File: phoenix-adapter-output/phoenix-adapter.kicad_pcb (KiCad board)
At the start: 2 copper layers, 16.2 x 20 mm, 2 parts, among them CON101 JST-XH

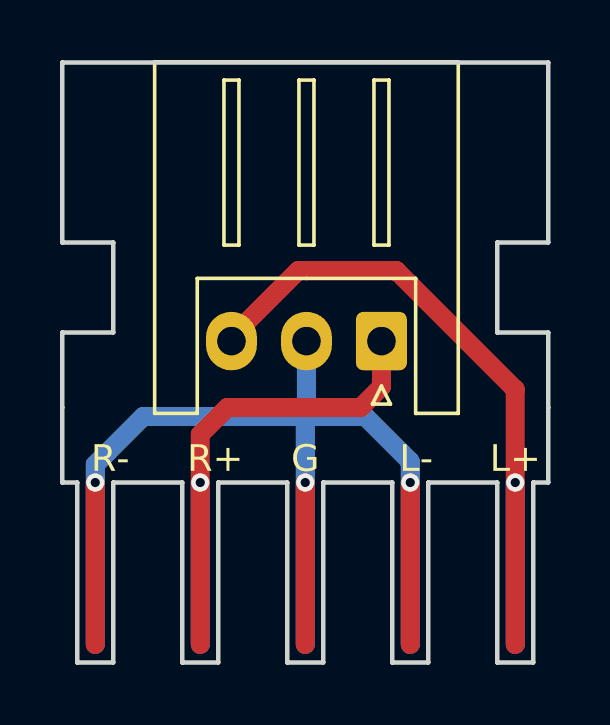
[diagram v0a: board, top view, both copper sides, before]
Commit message: added panel
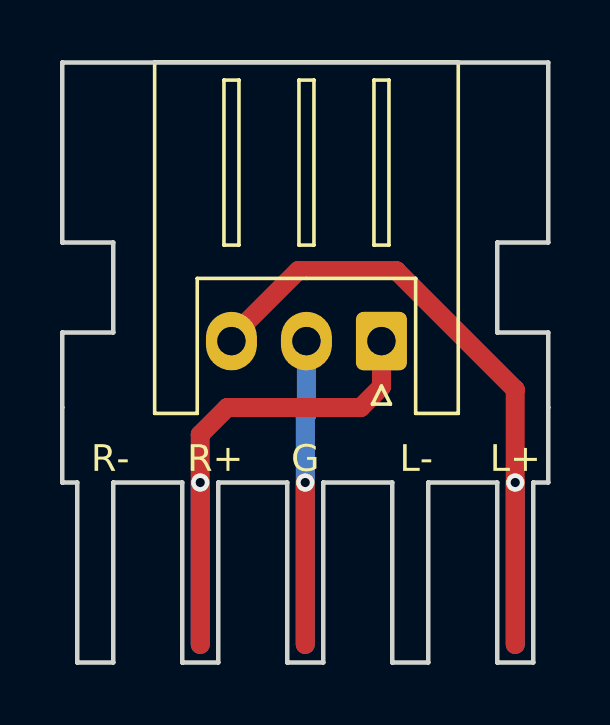
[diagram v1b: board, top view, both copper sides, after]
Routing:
- net GND: track 50.2 -> 15.5 mm, vias 3 -> 1
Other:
- board text added: "Output"
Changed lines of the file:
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@@
   (general
     (thickness 1.6)
-    (drawings 40)
-    (tracks 37)
+    (drawings 41)
+    (tracks 23)
     (zones 0)
     (modules 2)
@@
     )
   )
+  (gr_text Output (at 136.652 109.474) (layer B.SilkS)
+    (effects (font (size 1 1) (thickness 0.25)) (justify mirror))
+  )
   (gr_text db-electronics.ca (at 141.4 111.9) (layer B.SilkS)
     (effects (font (size 0.889 0.889) (thickness 0.2032)) (justify mirror))
@@
   (gr_line (start 131.6 113.3) (end 133.3 113.3) (layer Edge.Cuts) (width 0.15))
   (gr_line (start 131.6 107.3) (end 131.6 113.3) (layer Edge.Cuts) (width 0.15))
-  (segment (start 143.2 121.3) (end 143.2 126.7) (width 0.635) (layer F.Cu) (net 1))
-  (segment (start 143.2 121.3) (end 143.2 126.7) (width 0.635) (layer B.Cu) (net 1))
-  (segment (start 143.2 120.6) (end 143.2 121.3) (width 0.635) (layer B.Cu) (net 1))
-  (via (at 143.2 121.3) (size 0.6096) (drill 0.3048) (layers F.Cu B.Cu) (net 1))
   (segment (start 139.7 121.3) (end 139.7 126.7) (width 0.635) (layer F.Cu) (net 1))
   (segment (start 139.7 121.3) (end 139.7 126.7) (width 0.635) (layer B.Cu) (net 1))
   (segment (start 139.7 120.3) (end 139.7 121.3) (width 0.635) (layer B.Cu) (net 1))
   (via (at 139.7 121.3) (size 0.6096) (drill 0.3048) (layers F.Cu B.Cu) (net 1))
-  (segment (start 132.7 121.3) (end 132.7 126.7) (width 0.635) (layer F.Cu) (net 1))
-  (segment (start 132.7 121.3) (end 132.7 126.7) (width 0.635) (layer B.Cu) (net 1))
-  (segment (start 132.7 120.7) (end 132.7 121.3) (width 0.635) (layer B.Cu) (net 1))
-  (via (at 132.7 121.3) (size 0.6096) (drill 0.3048) (layers F.Cu B.Cu) (net 1))
-  (segment (start 142.9 120.3) (end 141.7 119.1) (width 0.635) (layer B.Cu) (net 1))
-  (segment (start 141.7 119.1) (end 139.7 119.1) (width 0.635) (layer B.Cu) (net 1))
   (segment (start 139.7 119.1) (end 139.7 120.3) (width 0.635) (layer B.Cu) (net 1))
-  (segment (start 133.1 120.3) (end 134.3 119.1) (width 0.635) (layer B.Cu) (net 1))
-  (segment (start 134.3 119.1) (end 139.7 119.1) (width 0.635) (layer B.Cu) (net 1))
-  (segment (start 133.1 120.3) (end 132.7 120.7) (width 0.635) (layer B.Cu) (net 1))
-  (segment (start 142.9 120.3) (end 143.2 120.6) (width 0.635) (layer B.Cu) (net 1))
   (segment (start 139.74 119.06) (end 139.74 116.586) (width 0.635) (layer B.Cu) (net 1))
   (segment (start 139.7 119.1) (end 139.74 119.06) (width 0.635) (layer B.Cu) (net 1))
@@
     (polygon
       (pts
-        (xy 132.1 122.3) (xy 132.1 127.3) (xy 133.3 127.3) (xy 133.3 122.3)
-      )
-    )
-  )
-  (zone (net 0) (net_name "") (layer F.Mask) (hatch edge 0.508)
-    (connect_pads (clearance 0.508))
-    (min_thickness 0.254)
-    (fill yes (arc_segments 16) (thermal_gap 0.508) (thermal_bridge_width 0.508))
-    (polygon
-      (pts
         (xy 135.6 122.3) (xy 135.6 127.3) (xy 136.8 127.3) (xy 136.8 122.3)
       )
@@
     (polygon
       (pts
-        (xy 142.6 122.3) (xy 142.6 127.3) (xy 143.8 127.3) (xy 143.8 122.3)
-      )
-    )
-  )
-  (zone (net 0) (net_name "") (layer F.Mask) (hatch edge 0.508)
-    (connect_pads (clearance 0.508))
-    (min_thickness 0.254)
-    (fill yes (arc_segments 16) (thermal_gap 0.508) (thermal_bridge_width 0.508))
-    (polygon
-      (pts
         (xy 146.1 122.3) (xy 146.1 127.3) (xy 147.3 127.3) (xy 147.3 122.3)
-      )
-    )
-  )
-  (zone (net 0) (net_name "") (layer B.Mask) (hatch edge 0.508)
-    (connect_pads (clearance 0.508))
-    (min_thickness 0.254)
-    (fill yes (arc_segments 16) (thermal_gap 0.508) (thermal_bridge_width 0.508))
-    (polygon
-      (pts
-        (xy 132.1 122.3) (xy 132.1 127.3) (xy 133.3 127.3) (xy 133.3 122.3)
       )
     )
@@
       )
     )
-  )
-  (zone (net 0) (net_name "") (layer B.Mask) (hatch edge 0.508)
-    (connect_pads (clearance 0.508))
-    (min_thickness 0.254)
-    (fill yes (arc_segments 16) (thermal_gap 0.508) (thermal_bridge_width 0.508))
-    (polygon
-      (pts
-        (xy 142.6 122.3) (xy 142.6 127.3) (xy 143.8 127.3) (xy 143.8 122.3)
-      )
-    )
